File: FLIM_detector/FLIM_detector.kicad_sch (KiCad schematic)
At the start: 8 parts

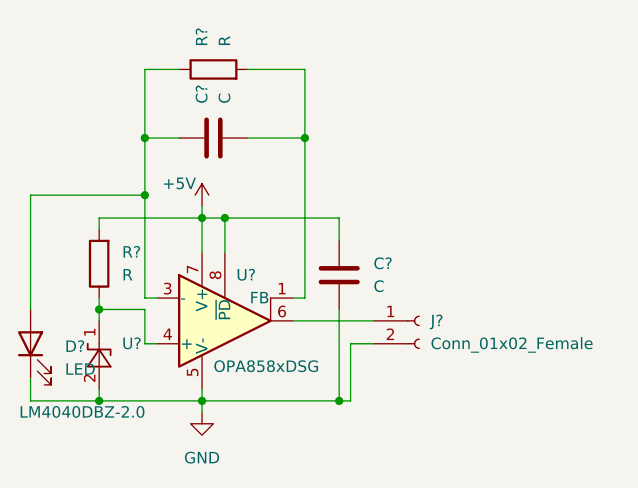
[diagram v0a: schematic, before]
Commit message: v0.2 components on PCB were decomposed
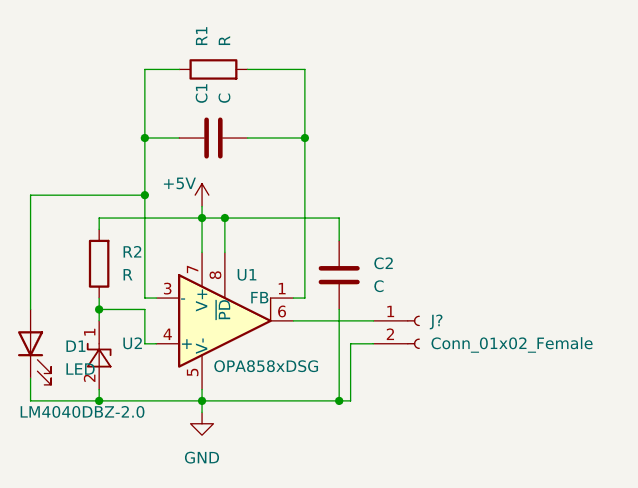
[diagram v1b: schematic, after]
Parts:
- removed J?: Conn_01x02_Female, symbol Connector:Conn_01x02_Female
- added J?: Conn_01x02_Female, Connector_PinHeader_2.54mm:PinHeader_1x02_P2.54mm_Vertical, symbol Connector:Conn_01x02_Female
- gave numbers to parts that had none: 7
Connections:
- net GND: now also J?.2 (Pin_2)
- net at U1.6: now also J?.1 (Pin_1)
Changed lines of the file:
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@@
     (stroke (width 0) (type default) (color 0 0 0 0))
   )
-  (symbol (lib_id "Connector:Conn_01x02_Female") (at 118.11 50.8 0) (unit 1)
-    (in_bom yes) (on_board yes) (fields_autoplaced)
-    (property "Reference" "J?" (id 0) (at 119.38 50.7999 0)
-      (effects (font (size 1.27 1.27)) (justify left))
-    )
-    (property "Value" "Conn_01x02_Female" (id 1) (at 119.38 53.3399 0)
-      (effects (font (size 1.27 1.27)) (justify left))
-    )
-    (property "Footprint" "" (id 2) (at 118.11 50.8 0)
-      (effects (font (size 1.27 1.27)) hide)
-    )
-    (property "Datasheet" "~" (id 3) (at 118.11 50.8 0)
-      (effects (font (size 1.27 1.27)) hide)
-    )
-    (pin "1")
-    (pin "2")
-  )
   (symbol (lib_id "power:GND") (at 93.98 60.96 0) (unit 1)
     (in_bom yes) (on_board yes) (fields_autoplaced)
-    (property "Reference" "#PWR?" (id 0) (at 93.98 67.31 0)
+    (property "Reference" "#PWR0101" (id 0) (at 93.98 67.31 0)
       (effects (font (size 1.27 1.27)) hide)
     )
@@
   (symbol (lib_id "Device:C") (at 109.22 45.72 180) (unit 1)
     (in_bom yes) (on_board yes) (fields_autoplaced)
-    (property "Reference" "C?" (id 0) (at 113.03 44.4499 0)
+    (property "Reference" "C2" (id 0) (at 113.03 44.4499 0)
       (effects (font (size 1.27 1.27)) (justify right))
     )
@@
   (symbol (lib_id "Device:C") (at 95.25 30.48 90) (unit 1)
     (in_bom yes) (on_board yes) (fields_autoplaced)
-    (property "Reference" "C?" (id 0) (at 93.9799 26.67 0)
+    (property "Reference" "C1" (id 0) (at 93.9799 26.67 0)
       (effects (font (size 1.27 1.27)) (justify left))
     )
@@
   (symbol (lib_id "Device:LED") (at 74.93 53.34 90) (unit 1)
     (in_bom yes) (on_board yes) (fields_autoplaced)
-    (property "Reference" "D?" (id 0) (at 78.74 53.6574 90)
+    (property "Reference" "D1" (id 0) (at 78.74 53.6574 90)
       (effects (font (size 1.27 1.27)) (justify right))
     )
@@
   (symbol (lib_id "Amplifier_Operational:OPA858xDSG") (at 96.52 50.8 0) (unit 1)
     (in_bom yes) (on_board yes)
-    (property "Reference" "U?" (id 0) (at 97.79 45.72 0)
+    (property "Reference" "U1" (id 0) (at 97.79 45.72 0)
       (effects (font (size 1.27 1.27)) (justify left))
     )
@@
   (symbol (lib_id "Device:R") (at 95.25 22.86 90) (unit 1)
     (in_bom yes) (on_board yes) (fields_autoplaced)
-    (property "Reference" "R?" (id 0) (at 93.9799 20.32 0)
+    (property "Reference" "R1" (id 0) (at 93.9799 20.32 0)
       (effects (font (size 1.27 1.27)) (justify left))
     )
@@
   (symbol (lib_id "power:+5V") (at 93.98 38.1 0) (unit 1)
     (in_bom yes) (on_board yes)
-    (property "Reference" "#PWR?" (id 0) (at 93.98 41.91 0)
+    (property "Reference" "#PWR0102" (id 0) (at 93.98 41.91 0)
       (effects (font (size 1.27 1.27)) hide)
     )
@@
     (pin "1")
   )
+  (symbol (lib_id "Connector:Conn_01x02_Female") (at 118.11 50.8 0) (unit 1)
+    (in_bom yes) (on_board yes) (fields_autoplaced)
+    (property "Reference" "J?" (id 0) (at 119.38 50.7999 0)
+      (effects (font (size 1.27 1.27)) (justify left))
+    )
+    (property "Value" "Conn_01x02_Female" (id 1) (at 119.38 53.3399 0)
+      (effects (font (size 1.27 1.27)) (justify left))
+    )
+    (property "Footprint" "Connector_PinHeader_2.54mm:PinHeader_1x02_P2.54mm_Vertical" (id 2) (at 118.11 50.8 0)
+      (effects (font (size 1.27 1.27)) hide)
+    )
+    (property "Datasheet" "~" (id 3) (at 118.11 50.8 0)
+      (effects (font (size 1.27 1.27)) hide)
+    )
+    (pin "1")
+    (pin "2")
+  )
   (symbol (lib_id "Device:R") (at 82.55 44.45 180) (unit 1)
     (in_bom yes) (on_board yes) (fields_autoplaced)
-    (property "Reference" "R?" (id 0) (at 85.09 43.1799 0)
+    (property "Reference" "R2" (id 0) (at 85.09 43.1799 0)
       (effects (font (size 1.27 1.27)) (justify right))
     )
@@
   (symbol (lib_id "Reference_Voltage:LM4040DBZ-2.0") (at 82.55 54.61 90) (unit 1)
     (in_bom yes) (on_board yes)
-    (property "Reference" "U?" (id 0) (at 85.09 53.3399 90)
+    (property "Reference" "U2" (id 0) (at 85.09 53.3399 90)
       (effects (font (size 1.27 1.27)) (justify right))
     )
@@
   (symbol_instances
     (path "/67199e20-af93-42e8-8ef6-fe0067df0a1c"
-      (reference "#PWR?") (unit 1) (value "GND") (footprint "")
+      (reference "#PWR0101") (unit 1) (value "GND") (footprint "")
     )
     (path "/d3e44f3c-4ea7-4046-87e4-ad4060de41af"
-      (reference "#PWR?") (unit 1) (value "+5V") (footprint "")
+      (reference "#PWR0102") (unit 1) (value "+5V") (footprint "")
+    )
+    (path "/8f40cd30-616e-41e2-bee9-266c3138b0af"
+      (reference "C1") (unit 1) (value "C") (footprint "Capacitor_SMD:C_0603_1608Metric_Pad1.08x0.95mm_HandSolder")
     )
     (path "/6fbf5a8c-1d4d-40c4-b8e3-d93886b1fd05"
-      (reference "C?") (unit 1) (value "C") (footprint "Capacitor_SMD:C_0603_1608Metric_Pad1.08x0.95mm_HandSolder")
-    )
-    (path "/8f40cd30-616e-41e2-bee9-266c3138b0af"
-      (reference "C?") (unit 1) (value "C") (footprint "Capacitor_SMD:C_0603_1608Metric_Pad1.08x0.95mm_HandSolder")
+      (reference "C2") (unit 1) (value "C") (footprint "Capacitor_SMD:C_0603_1608Metric_Pad1.08x0.95mm_HandSolder")
     )
     (path "/ad354e5c-56b2-4aad-b249-1c4acb12831e"
-      (reference "D?") (unit 1) (value "LED") (footprint "LED_THT:LED_D5.0mm_Clear")
-    )
-    (path "/1c4eb6ea-5a83-4bf0-90fe-eb0b775bdda3"
-      (reference "J?") (unit 1) (value "Conn_01x02_Female") (footprint "")
+      (reference "D1") (unit 1) (value "LED") (footprint "LED_THT:LED_D5.0mm_Clear")
+    )
+    (path "/ddf345f3-957b-415e-835e-ca7082def9c0"
+      (reference "J?") (unit 1) (value "Conn_01x02_Female") (footprint "Connector_PinHeader_2.54mm:PinHeader_1x02_P2.54mm_Vertical")
     )
     (path "/d1e09193-4976-4c3a-ad43-78fdc2586714"
-      (reference "R?") (unit 1) (value "R") (footprint "Resistor_SMD:R_0603_1608Metric_Pad0.98x0.95mm_HandSolder")
+      (reference "R1") (unit 1) (value "R") (footprint "Resistor_SMD:R_0603_1608Metric_Pad0.98x0.95mm_HandSolder")
     )
     (path "/f708eeca-2978-4dd9-9197-ffaf4e5e7409"
-      (reference "R?") (unit 1) (value "R") (footprint "Resistor_SMD:R_0603_1608Metric_Pad0.98x0.95mm_HandSolder")
+      (reference "R2") (unit 1) (value "R") (footprint "Resistor_SMD:R_0603_1608Metric_Pad0.98x0.95mm_HandSolder")
     )
     (path "/be5a7017-fe9d-43ea-9a6a-8fe8deb78420"
-      (reference "U?") (unit 1) (value "OPA858xDSG") (footprint "Package_SON:WSON-8-1EP_2x2mm_P0.5mm_EP0.9x1.6mm_ThermalVias")
+      (reference "U1") (unit 1) (value "OPA858xDSG") (footprint "Package_SON:WSON-8-1EP_2x2mm_P0.5mm_EP0.9x1.6mm_ThermalVias")
     )
     (path "/f9242bfa-8da4-4b4e-b2b4-9b0d539538f3"
-      (reference "U?") (unit 1) (value "LM4040DBZ-2.0") (footprint "Package_TO_SOT_SMD:SOT-23")
-    )
-  )
+      (reference "U2") (unit 1) (value "LM4040DBZ-2.0") (footprint "Package_TO_SOT_SMD:SOT-23")
+    )
+  )

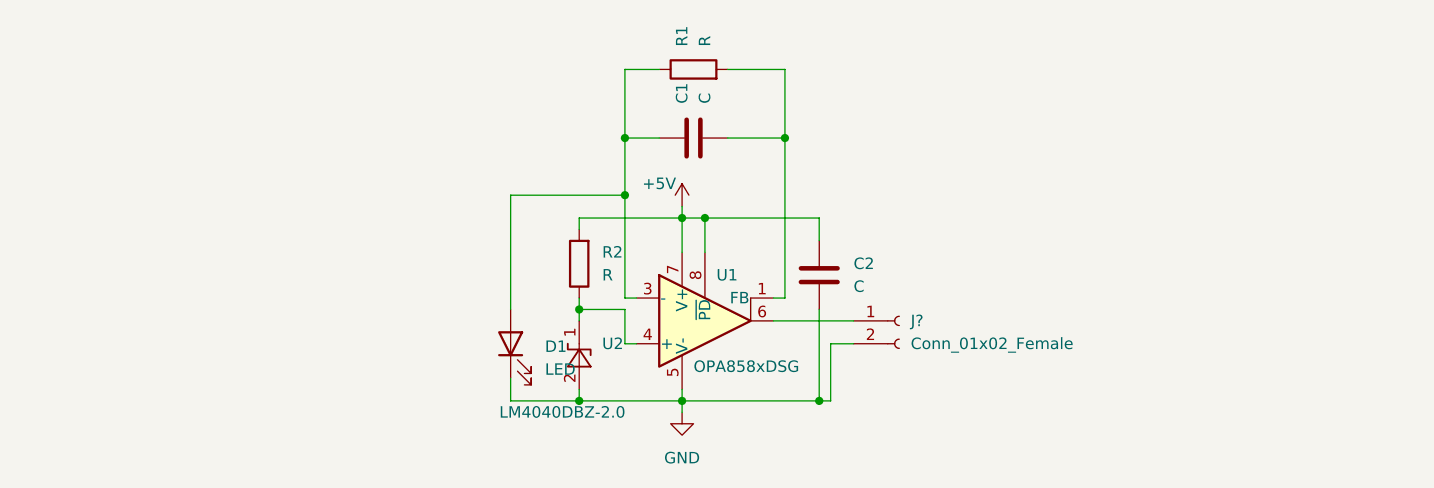
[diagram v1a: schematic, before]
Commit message: v0.3 power source waas added, some components were decreased into 0402
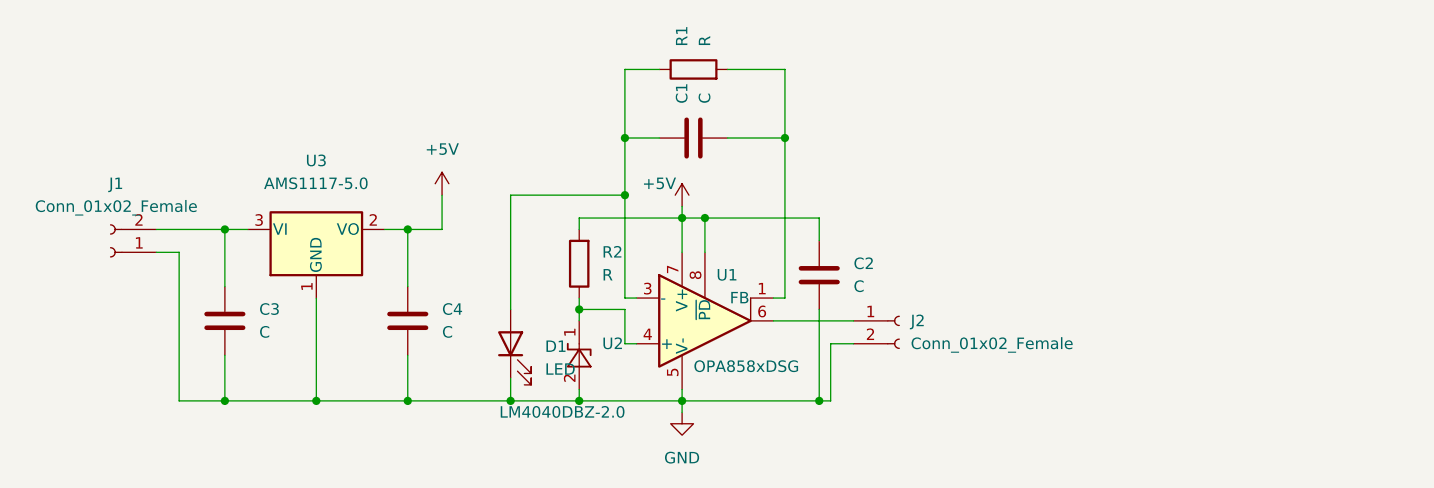
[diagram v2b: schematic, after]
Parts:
- added C3, C4: C, Capacitor_SMD:C_0603_1608Metric_Pad1.08x0.95mm_HandSolder, symbol Device:C
- added J1: Conn_01x02_Female, Connector_PinHeader_2.54mm:PinHeader_1x02_P2.54mm_Vertical, symbol Connector:Conn_01x02_Female
- added U3: AMS1117-5.0, Package_TO_SOT_SMD:SOT-223-3_TabPin2, symbol Regulator_Linear:AMS1117-5.0
- C1, C2: footprint Capacitor_SMD:C_0603_1608Metric_Pad1.08x0.95mm_HandSolder -> Capacitor_SMD:C_0402_1005Metric_Pad0.74x0.62mm_HandSolder
- R1, R2: footprint Resistor_SMD:R_0603_1608Metric_Pad0.98x0.95mm_HandSolder -> Resistor_SMD:R_0402_1005Metric_Pad0.72x0.64mm_HandSolder
- gave numbers to parts that had none: 1
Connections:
- net +5V: now also C4.2, U3.2 (VO)
- net GND: now also C3.1, C4.1, J1.1 (Pin_1), U3.1 (GND)
- new net: C3.2, J1.2 (Pin_2), U3.3 (VI)

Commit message: v0.4 input shotthy was added
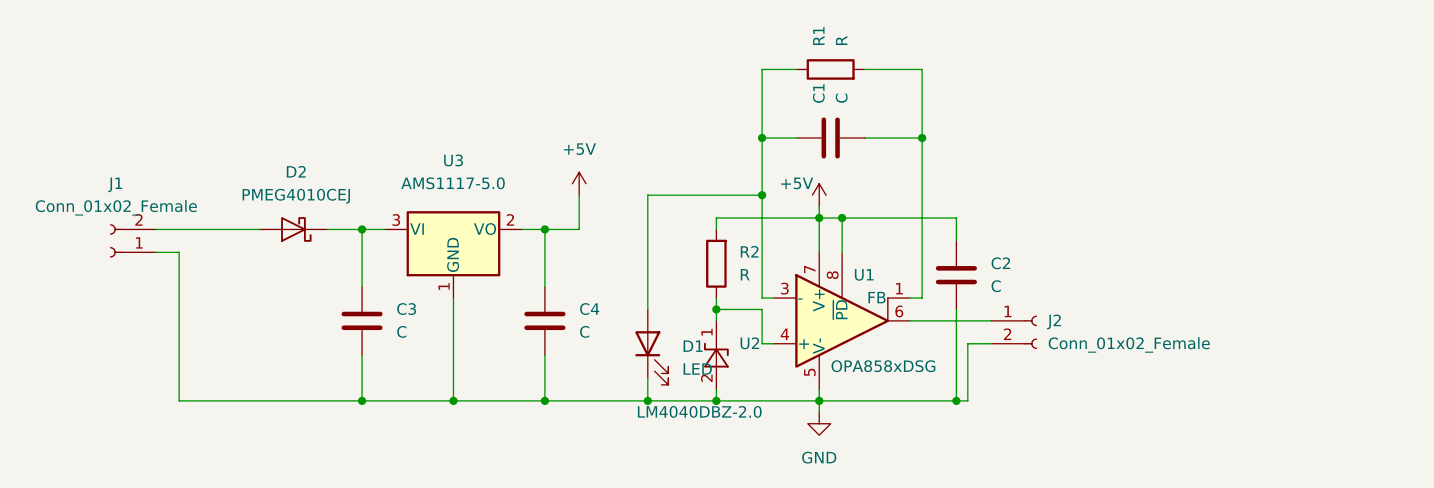
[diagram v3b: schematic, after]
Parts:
- added D2: PMEG4010CEJ, Diode_SMD:D_SOD-323F, symbol Diode:PMEG4010CEJ
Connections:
- net at C3.2, U3.3 (VI): now also D2.1 (K); no longer J1.2 (Pin_2)
- new net: D2.2 (A), J1.2 (Pin_2)
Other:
- moved on the sheet: C1, C2, C3, C4, D1, J2, R1, R2, U1, U2, U3

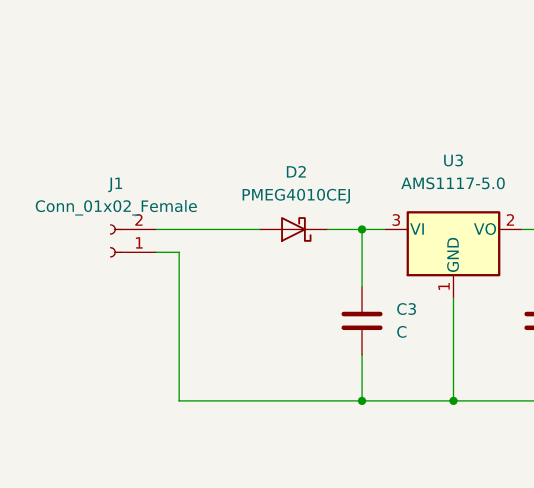
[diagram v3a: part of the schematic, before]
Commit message: v0.7 power connector was flipped
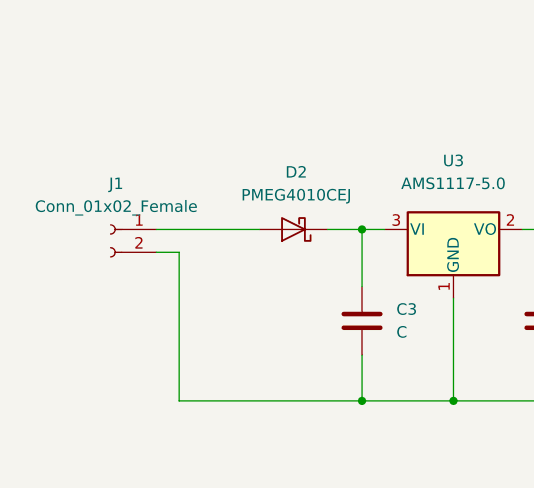
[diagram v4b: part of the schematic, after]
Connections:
- net GND: now also J1.2 (Pin_2); no longer J1.1 (Pin_1)
- net at D2.2 (A): now also J1.1 (Pin_1); no longer J1.2 (Pin_2)
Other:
- moved on the sheet: J1
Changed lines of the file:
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@@
-    (stroke (width 0) (type default) (color 0 0 0 0))
-  )
-  (wire (pts (xy 35.56 43.18) (xy 38.1 43.18))
     (stroke (width 0) (type default) (color 0 0 0 0))
   )
@@
     (stroke (width 0) (type default) (color 0 0 0 0))
   )
+  (wire (pts (xy 35.56 43.18) (xy 38.1 43.18))
+    (stroke (width 0) (type default) (color 0 0 0 0))
+  )
   (wire (pts (xy 120.65 48.26) (xy 119.38 48.26))
     (stroke (width 0) (type default) (color 0 0 0 0))
@@
     (stroke (width 0) (type default) (color 0 0 0 0))
   )
-  (symbol (lib_id "Connector:Conn_01x02_Female") (at 30.48 43.18 180) (unit 1)
+  (symbol (lib_id "Connector:Conn_01x02_Female") (at 30.48 40.64 0) (mirror y) (unit 1)
     (in_bom yes) (on_board yes) (fields_autoplaced)
     (property "Reference" "J1" (id 0) (at 31.115 35.56 0))
     (property "Value" "Conn_01x02_Female" (id 1) (at 31.115 38.1 0))
-    (property "Footprint" "Connector_PinHeader_2.54mm:PinHeader_1x02_P2.54mm_Vertical" (id 2) (at 30.48 43.18 0)
+    (property "Footprint" "Connector_PinHeader_2.54mm:PinHeader_1x02_P2.54mm_Vertical" (id 2) (at 30.48 40.64 0)
       (effects (font (size 1.27 1.27)) hide)
     )
-    (property "Datasheet" "~" (id 3) (at 30.48 43.18 0)
+    (property "Datasheet" "~" (id 3) (at 30.48 40.64 0)
       (effects (font (size 1.27 1.27)) hide)
     )

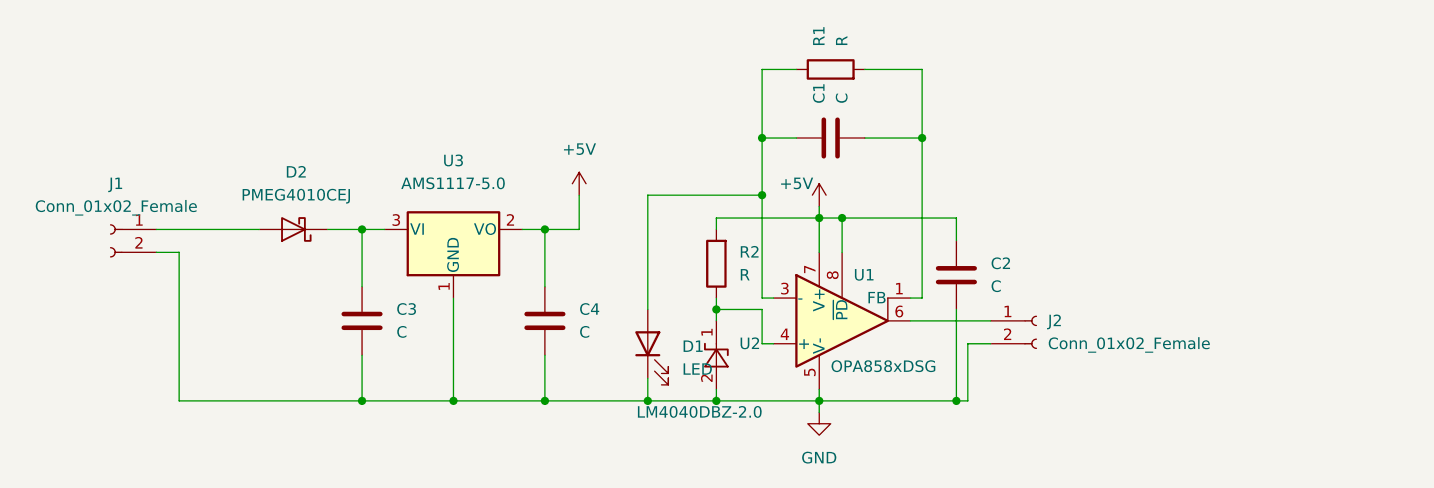
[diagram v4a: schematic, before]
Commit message: v0.8 Routing was optimized
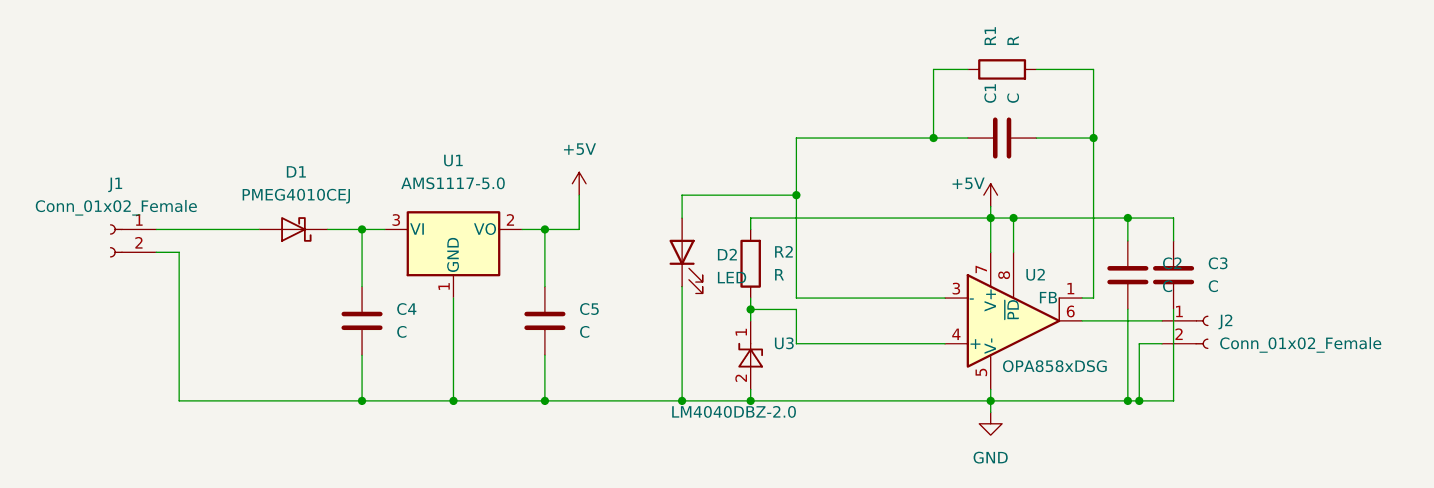
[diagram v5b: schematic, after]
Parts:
- added C3: C, Capacitor_SMD:C_0201_0603Metric, symbol Device:C
- C1, C2: footprint Capacitor_SMD:C_0402_1005Metric_Pad0.74x0.62mm_HandSolder -> Capacitor_SMD:C_0201_0603Metric
- R1: footprint Resistor_SMD:R_0402_1005Metric_Pad0.72x0.64mm_HandSolder -> Resistor_SMD:R_0201_0603Metric
- renumbered C3 to C4, C4 to C5, D2 to D1, D1 to D2, U3 to U1, U1 to U2, U2 to U3
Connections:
- net +5V: now also C3.2
- net GND: now also C3.1
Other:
- moved on the sheet: C1, C2, D2, J2, R1, R2, U2, U3
